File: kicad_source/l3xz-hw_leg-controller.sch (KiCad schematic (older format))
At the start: 18 parts, among them CN1 ARDUINO_NANO_33, CN2 CONN_01X04, CN3 CONN_02X03, P1 CONN_01X02, U3 24LC64

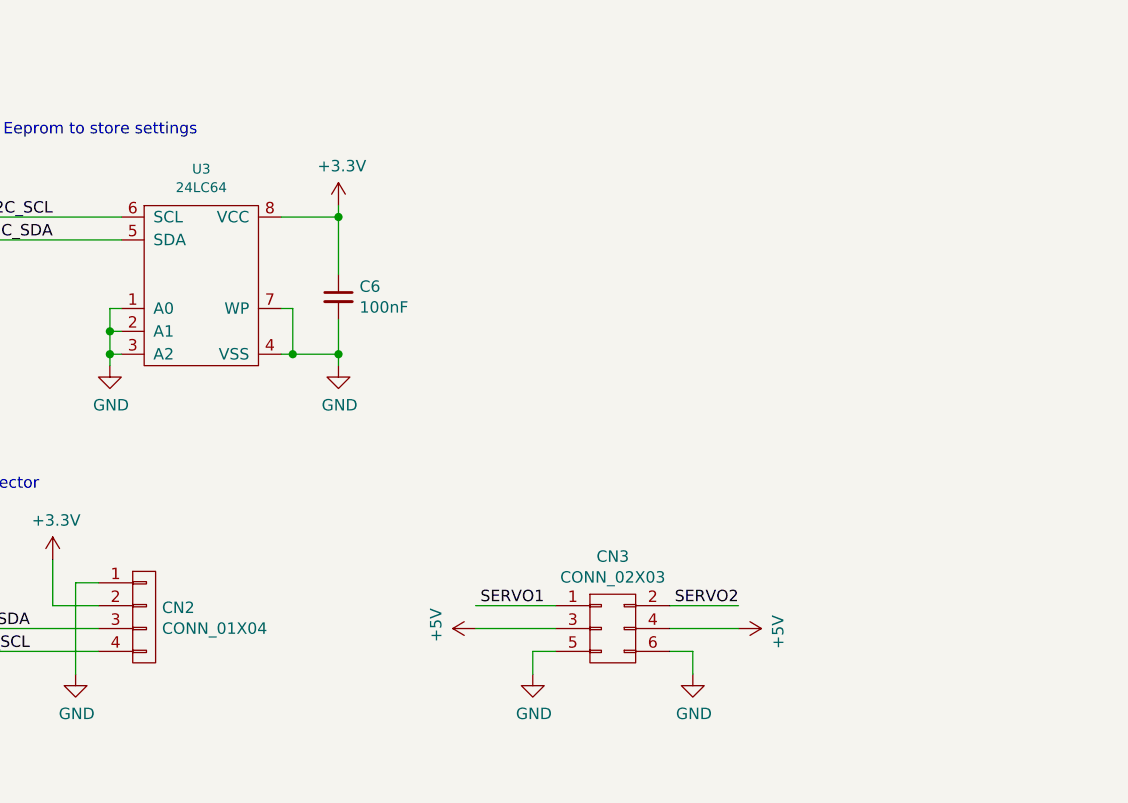
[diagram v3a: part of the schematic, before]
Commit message: updated schematic, corrected connector designators, updated footprints
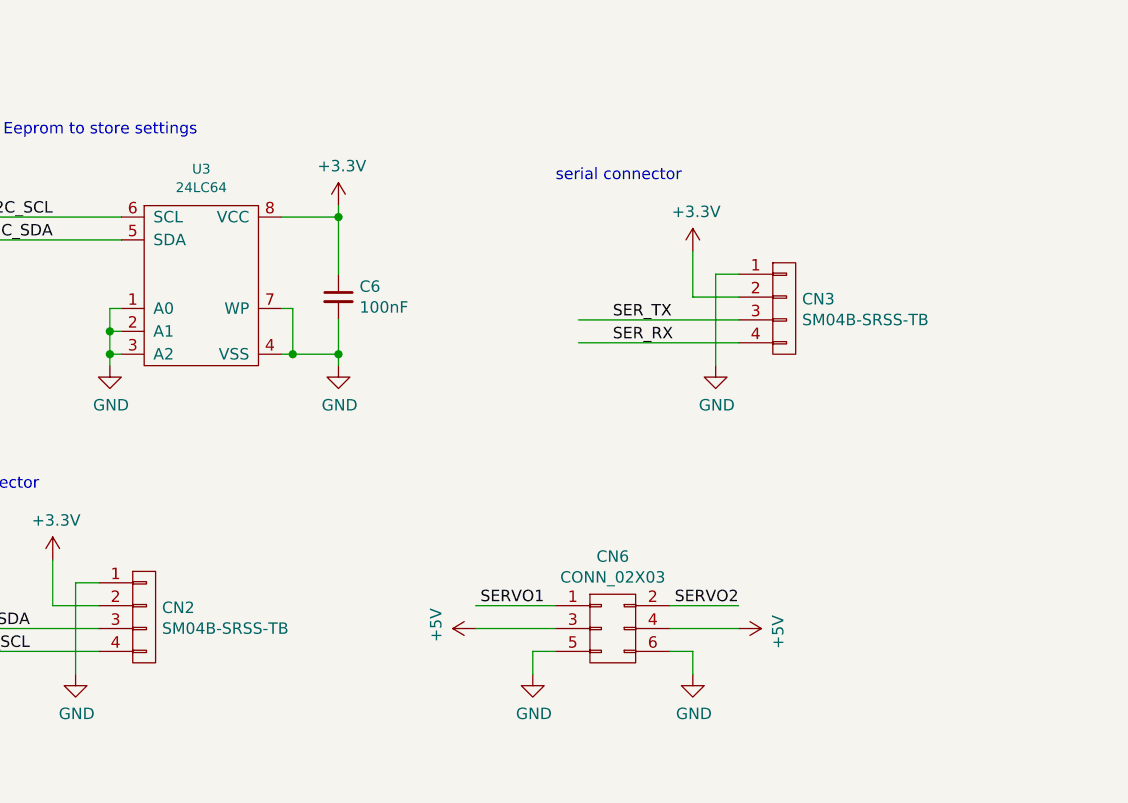
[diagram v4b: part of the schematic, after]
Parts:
- added CN3: SM04B-SRSS-TB, connectors_JST_SH:Connectors_JST_SM04B-SRSS-TB, symbol mechanical-connectors:CONN_01X04
- CN2: value CONN_01X04 -> SM04B-SRSS-TB; footprint (none) -> connectors_JST_SH:Connectors_JST_SM04B-SRSS-TB
- CN6: renamed from CN3; footprint (none) -> pin_headers:Pin_Header_Angled_2x03
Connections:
- wire segments 67 -> 73
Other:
- note added: "serial connector"
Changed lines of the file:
@@
 BUMPER
-$Comp
-L mechanical-connectors:CONN_01X04 CN2
-U 1 1 6250C797
-P 2000 6350
-F 0 "CN2" H 2078 6391 50  0000 L CNN
-F 1 "CONN_01X04" H 2078 6300 50  0000 L CNN
-F 2 "" H 2000 6350 50  0000 C CNN
-F 3 "" H 2000 6350 50  0000 C CNN
-	1    2000 6350
-	1    0    0    -1
-$EndComp
 $Comp
 L power-supply:GND #PWR031
@@
 qwiic connector
 $Comp
-L mechanical-connectors:CONN_02X03 CN3
+L mechanical-connectors:CONN_02X03 CN6
 U 1 1 624F7225
 P 4050 6400
-F 0 "CN3" H 4050 6715 50  0000 C CNN
+F 0 "CN6" H 4050 6715 50  0000 C CNN
 F 1 "CONN_02X03" H 4050 6624 50  0000 C CNN
-F 2 "" H 4050 5200 50  0000 C CNN
+F 2 "pin_headers:Pin_Header_Angled_2x03" H 4050 5200 50  0001 C CNN
 F 3 "" H 4050 5200 50  0000 C CNN
 	1    4050 6400
@@
 Text Notes 1250 4250 0    50   ~ 0
 I2C Eeprom to store settings
+$Comp
+L mechanical-connectors:CONN_01X04 CN3
+U 1 1 6250779D
+P 4800 5000
+F 0 "CN3" H 4878 5041 50  0000 L CNN
+F 1 "SM04B-SRSS-TB" H 4878 4950 50  0000 L CNN
+F 2 "connectors_JST_SH:Connectors_JST_SM04B-SRSS-TB" H 4800 5000 50  0001 C CNN
+F 3 "" H 4800 5000 50  0000 C CNN
+	1    4800 5000
+	1    0    0    -1
+$EndComp
+$Comp
+L power-supply:GND #PWR040
+U 1 1 625078B1
+P 4500 5250
+F 0 "#PWR040" H 4500 5000 50  0001 C CNN
+F 1 "GND" H 4505 5077 50  0000 C CNN
+F 2 "" H 4500 5250 50  0000 C CNN
+F 3 "" H 4500 5250 50  0000 C CNN
+	1    4500 5250
+	1    0    0    -1
+$EndComp
+$Comp
+L power-supply:+3.3V #PWR?
+U 1 1 625078BB
+P 4400 4750
+AR Path="/5ED92F9C/625078BB" Ref="#PWR?"  Part="1"
+AR Path="/625078BB" Ref="#PWR039"  Part="1"
+F 0 "#PWR039" H 4400 4600 50  0001 C CNN
+F 1 "+3.3V" H 4415 4923 50  0000 C CNN
+F 2 "" H 4400 4750 50  0000 C CNN
+F 3 "" H 4400 4750 50  0000 C CNN
+	1    4400 4750
+	1    0    0    -1
+$EndComp
+Wire Wire Line
+	4600 4950 4400 4950
+Wire Wire Line
+	4400 4950 4400 4750
+Wire Wire Line
+	4600 4850 4500 4850
+Wire Wire Line
+	4500 4850 4500 5250
+Wire Wire Line
+	3900 5050 4600 5050
+Wire Wire Line
+	3900 5150 4600 5150
+Text Notes 3800 4450 0    50   ~ 0
+serial connector
+Text Label 4050 5050 0    50   ~ 0
+SER_TX
+Text Label 4050 5150 0    50   ~ 0
+SER_RX
+$Comp
+L mechanical-connectors:CONN_01X04 CN2
+U 1 1 6250DED9
+P 2000 6350
+F 0 "CN2" H 2078 6391 50  0000 L CNN
+F 1 "SM04B-SRSS-TB" H 2078 6300 50  0000 L CNN
+F 2 "connectors_JST_SH:Connectors_JST_SM04B-SRSS-TB" H 2000 6350 50  0001 C CNN
+F 3 "" H 2000 6350 50  0000 C CNN
+	1    2000 6350
+	1    0    0    -1
+$EndComp
 $EndSCHEMATC

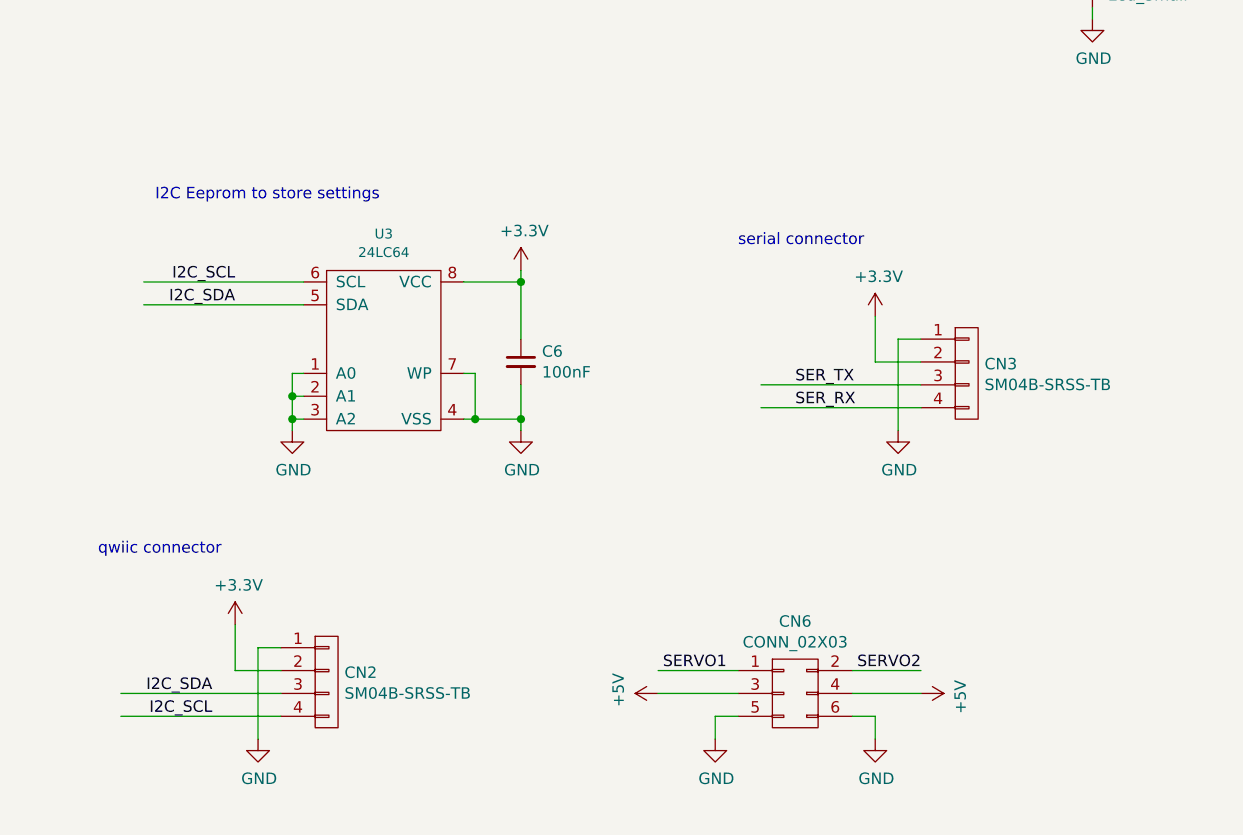
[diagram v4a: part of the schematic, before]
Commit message: added pull up to i2c, serial resistor to servo
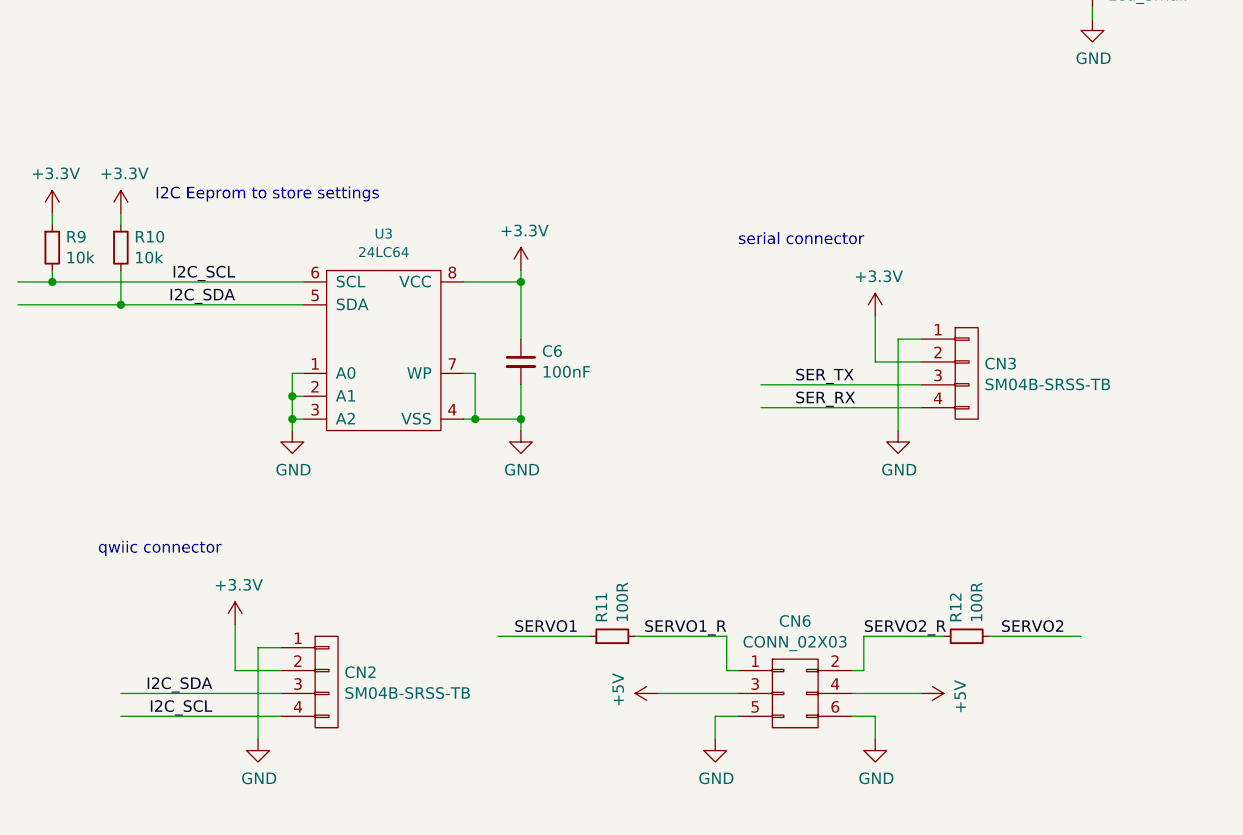
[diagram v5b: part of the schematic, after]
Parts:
- added R10, R9: 10k, resistors:R_0603, symbol devices:R_0603
- added R11, R12: 100R, resistors:R_0603, symbol devices:R_0603
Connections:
- net labels added: SERVO1_R, SERVO2_R
- wire segments 73 -> 85
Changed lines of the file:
@@
 Wire Wire Line
 	3450 6400 3800 6400
-Wire Wire Line
-	3450 6300 3800 6300
-Wire Wire Line
-	4600 6300 4300 6300
-Text Label 3750 6300 2    50   ~ 0
+Text Label 3100 6150 2    50   ~ 0
 SERVO1
-Text Label 4600 6300 2    50   ~ 0
+Text Label 4950 6150 0    50   ~ 0
 SERVO2
 Wire Wire Line
@@
 Wire Wire Line
 	2650 5200 2850 5200
-Wire Wire Line
-	1200 4600 1900 4600
-Wire Wire Line
-	1200 4700 1900 4700
 Text Label 1600 4700 2    50   ~ 0
 I2C_SDA
@@
 	1    0    0    -1
 $EndComp
+$Comp
+L devices:R_0603 R?
+U 1 1 62508159
+P 800 4450
+AR Path="/5ED92F9C/62508159" Ref="R?"  Part="1"
+AR Path="/62508159" Ref="R9"  Part="1"
+F 0 "R9" H 859 4496 50  0000 L CNN
+F 1 "10k" H 859 4405 50  0000 L CNN
+F 2 "resistors:R_0603" H 800 4300 50  0001 C CNN
+F 3 "" H 800 4450 50  0000 C CNN
+	1    800  4450
+	1    0    0    -1
+$EndComp
+$Comp
+L devices:R_0603 R?
+U 1 1 62509863
+P 1100 4450
+AR Path="/5ED92F9C/62509863" Ref="R?"  Part="1"
+AR Path="/62509863" Ref="R10"  Part="1"
+F 0 "R10" H 1159 4496 50  0000 L CNN
+F 1 "10k" H 1159 4405 50  0000 L CNN
+F 2 "resistors:R_0603" H 1100 4300 50  0001 C CNN
+F 3 "" H 1100 4450 50  0000 C CNN
+	1    1100 4450
+	1    0    0    -1
+$EndComp
+$Comp
+L power-supply:+3.3V #PWR?
+U 1 1 62509BD1
+P 800 4300
+AR Path="/5ED92F9C/62509BD1" Ref="#PWR?"  Part="1"
+AR Path="/62509BD1" Ref="#PWR041"  Part="1"
+F 0 "#PWR041" H 800 4150 50  0001 C CNN
+F 1 "+3.3V" H 815 4473 50  0000 C CNN
+F 2 "" H 800 4300 50  0000 C CNN
+F 3 "" H 800 4300 50  0000 C CNN
+	1    800  4300
+	1    0    0    -1
+$EndComp
+$Comp
+L power-supply:+3.3V #PWR?
+U 1 1 62509F54
+P 1100 4300
+AR Path="/5ED92F9C/62509F54" Ref="#PWR?"  Part="1"
+AR Path="/62509F54" Ref="#PWR042"  Part="1"
+F 0 "#PWR042" H 1100 4150 50  0001 C CNN
+F 1 "+3.3V" H 1115 4473 50  0000 C CNN
+F 2 "" H 1100 4300 50  0000 C CNN
+F 3 "" H 1100 4300 50  0000 C CNN
+	1    1100 4300
+	1    0    0    -1
+$EndComp
+Wire Wire Line
+	650  4600 800  4600
+Wire Wire Line
+	650  4700 1100 4700
+Wire Wire Line
+	800  4300 800  4350
+Wire Wire Line
+	1100 4300 1100 4350
+Wire Wire Line
+	800  4550 800  4600
+Connection ~ 800  4600
+Wire Wire Line
+	800  4600 1900 4600
+Wire Wire Line
+	1100 4550 1100 4700
+Connection ~ 1100 4700
+Wire Wire Line
+	1100 4700 1900 4700
+$Comp
+L devices:R_0603 R?
+U 1 1 62518752
+P 4800 6150
+AR Path="/5ED92F9C/62518752" Ref="R?"  Part="1"
+AR Path="/62518752" Ref="R12"  Part="1"
+F 0 "R12" H 4859 6196 50  0000 L CNN
+F 1 "100R" H 4859 6105 50  0000 L CNN
+F 2 "resistors:R_0603" H 4800 6000 50  0001 C CNN
+F 3 "" H 4800 6150 50  0000 C CNN
+	1    4800 6150
+	0    -1   -1   0
+$EndComp
+$Comp
+L devices:R_0603 R?
+U 1 1 625199DA
+P 3250 6150
+AR Path="/5ED92F9C/625199DA" Ref="R?"  Part="1"
+AR Path="/625199DA" Ref="R11"  Part="1"
+F 0 "R11" H 3309 6196 50  0000 L CNN
+F 1 "100R" H 3309 6105 50  0000 L CNN
+F 2 "resistors:R_0603" H 3250 6000 50  0001 C CNN
+F 3 "" H 3250 6150 50  0000 C CNN
+	1    3250 6150
+	0    -1   -1   0
+$EndComp
+Wire Wire Line
+	5300 6150 4900 6150
+Wire Wire Line
+	2750 6150 3150 6150
+Wire Wire Line
+	3350 6150 3750 6150
+Wire Wire Line
+	3750 6150 3750 6300
+Wire Wire Line
+	3750 6300 3800 6300
+Wire Wire Line
+	4350 6150 4350 6300
+Wire Wire Line
+	4350 6300 4300 6300
+Wire Wire Line
+	4350 6150 4700 6150
+Text Label 4350 6150 0    50   ~ 0
+SERVO2_R
+Text Label 3750 6150 2    50   ~ 0
+SERVO1_R
 $EndSCHEMATC
